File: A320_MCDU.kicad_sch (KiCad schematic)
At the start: 0 parts

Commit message: Finished all button
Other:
- added sheet Pico (pico.kicad_sch)
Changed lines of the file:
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@@
 	(paper "A4")
+	(sheet
+		(at 113.03 92.71)
+		(size 16.51 3.81)
+		(exclude_from_sim no)
+		(in_bom yes)
+		(on_board yes)
+		(dnp no)
+		(fields_autoplaced yes)
+		(stroke
+			(width 0.1524)
+			(type solid)
+		)
+		(fill
+			(color 0 0 0 0)
+		)
+		(property "Sheetname" "Pico"
+			(at 113.03 91.9984 0)
+			(show_name no)
+			(do_not_autoplace no)
+			(effects
+				(font
+					(size 1.27 1.27)
+				)
+				(justify left bottom)
+			)
+		)
+		(property "Sheetfile" "pico.kicad_sch"
+			(at 113.03 97.1046 0)
+			(show_name no)
+			(do_not_autoplace no)
+			(effects
+				(font
+					(size 1.27 1.27)
+				)
+				(justify left top)
+			)
+		)
+		(instances
+			(project "A320_MCDU"
+				(path "/389a66ff-e1cc-4543-98a7-e36fba49f9f6"
+					(page "5")
+				)
+			)
+		)
+	)
 	(sheet
 		(at 132.08 60.96)

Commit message: add: TODO
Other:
- note added: "TODO: Pico part (all connection)"
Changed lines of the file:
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@@
 	(generator_version "10.0")
 	(paper "A4")
+	(text "TODO: Pico part (all connection)"
+		(exclude_from_sim no)
+		(at 121.92 101.6 0)
+		(effects
+			(font
+				(size 1.27 1.27)
+			)
+		)
+	)
 	(sheet
 		(at 113.03 92.71)

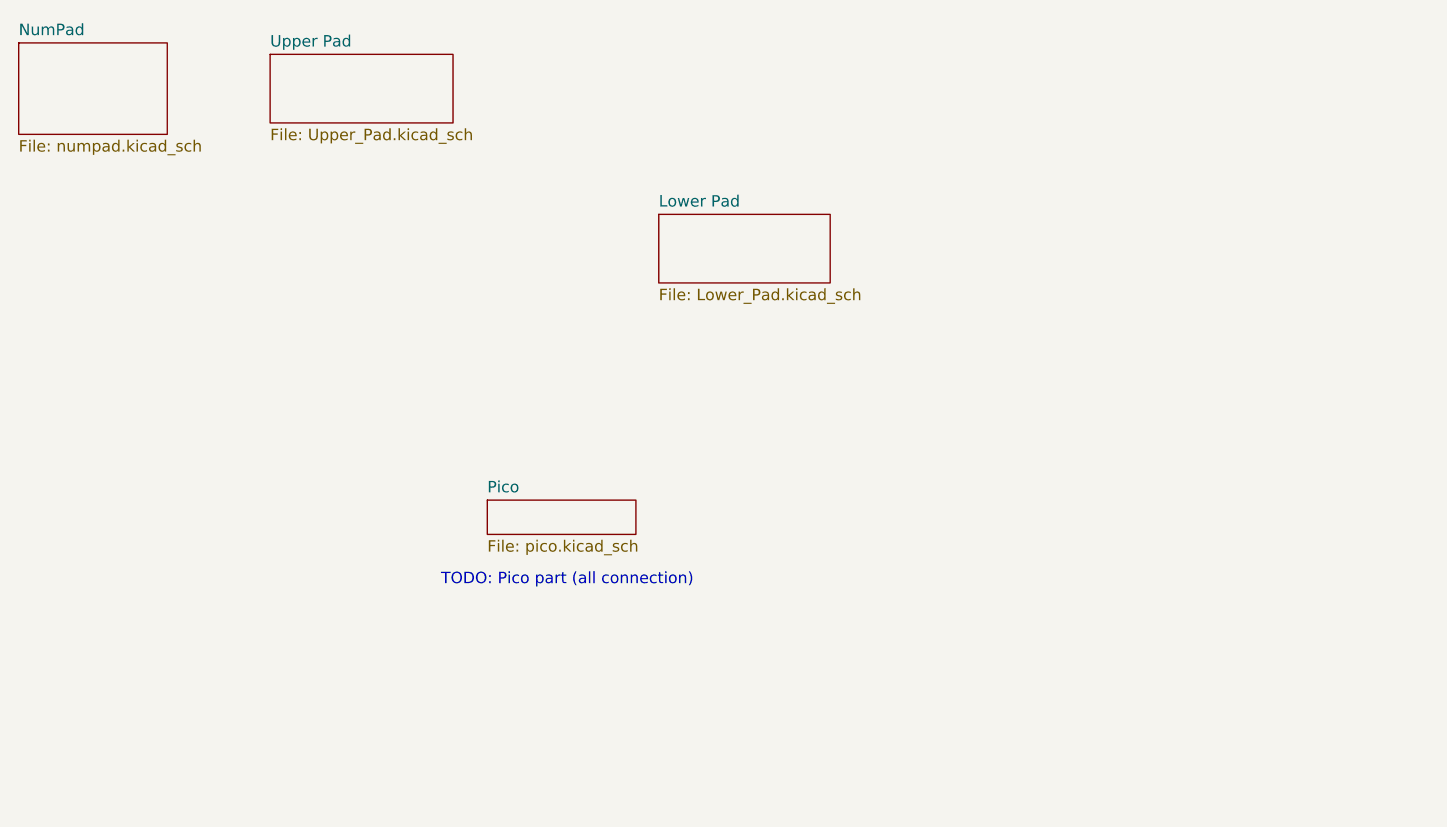
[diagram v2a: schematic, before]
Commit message: Add: PCB Part, NumPad Mesurement
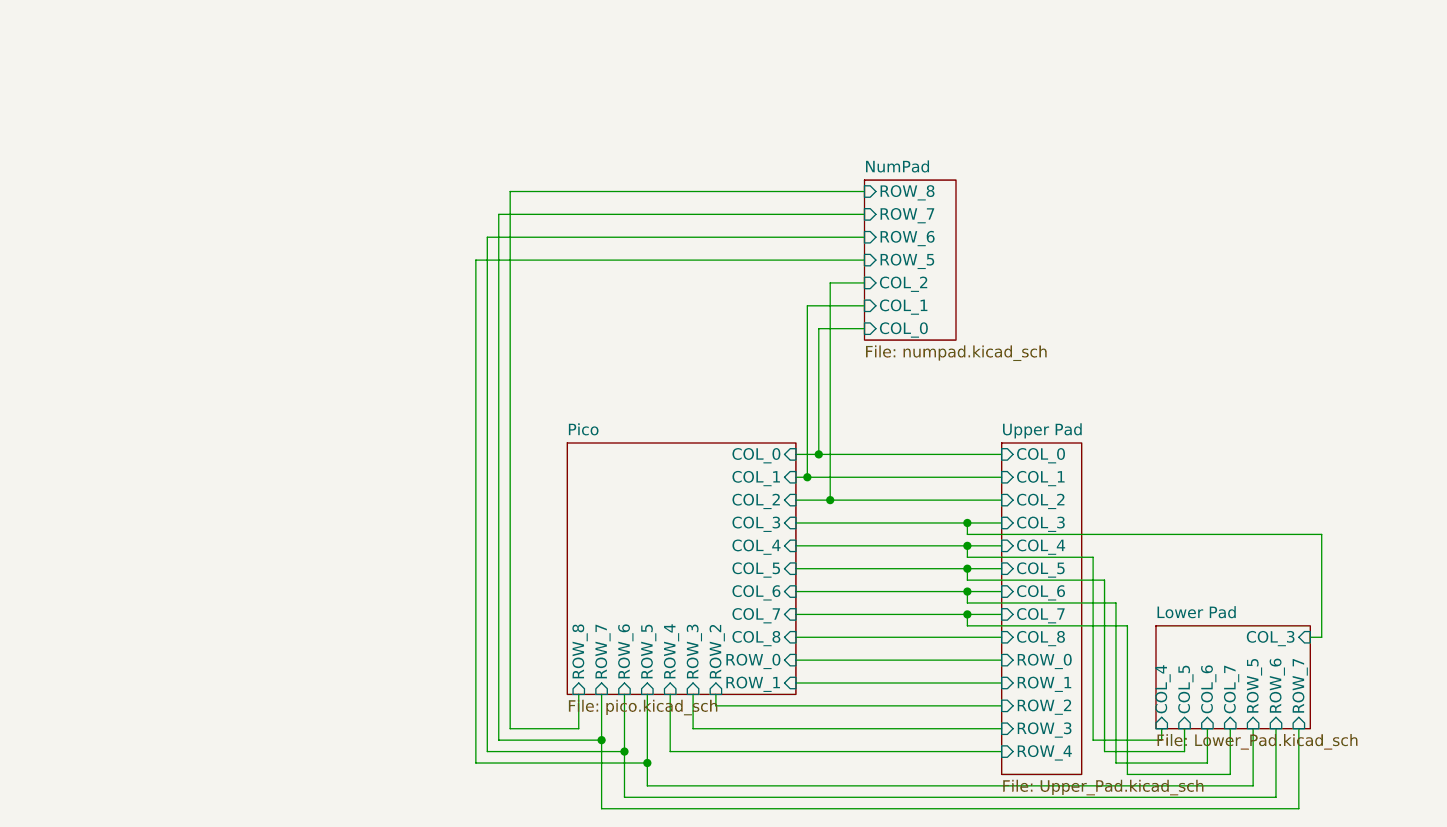
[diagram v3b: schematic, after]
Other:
- sheet Lower Pad ports: added COL_3, COL_4, COL_5, COL_6, COL_7, ROW_5, ROW_6, ROW_7; removed none
- sheet NumPad ports: added COL_0, COL_1, COL_2, ROW_5, ROW_6, ROW_7, ROW_8; removed none
- sheet Pico ports: added COL_0, COL_1, COL_2, COL_3, COL_4, COL_5, COL_6, COL_7, COL_8, ROW_0, ROW_1, ROW_2, ROW_3, ROW_4, ROW_5, ROW_6, ROW_7, ROW_8; removed none
- sheet Upper Pad ports: added COL_0, COL_1, COL_2, COL_3, COL_4, COL_5, COL_6, COL_7, COL_8, ROW_0, ROW_1, ROW_2, ROW_3, ROW_4; removed none
- note removed: "TODO: Pico part (all connection)"
